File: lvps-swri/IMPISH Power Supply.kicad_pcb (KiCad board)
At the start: 4 copper layers, 90 x 90 mm, 68 parts, among them J1 Battery +, J2 Battery +, J3 Battery -, J4 Battery -, J5 BCS-117-L-D-TE, U1 PXG-M15-24WS05, U2 CCG30-24-12S, U3 PXC-M03-24WD15-A, U4 PXC-M03-24WS05-A, U5 PXG-M15-24WD05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

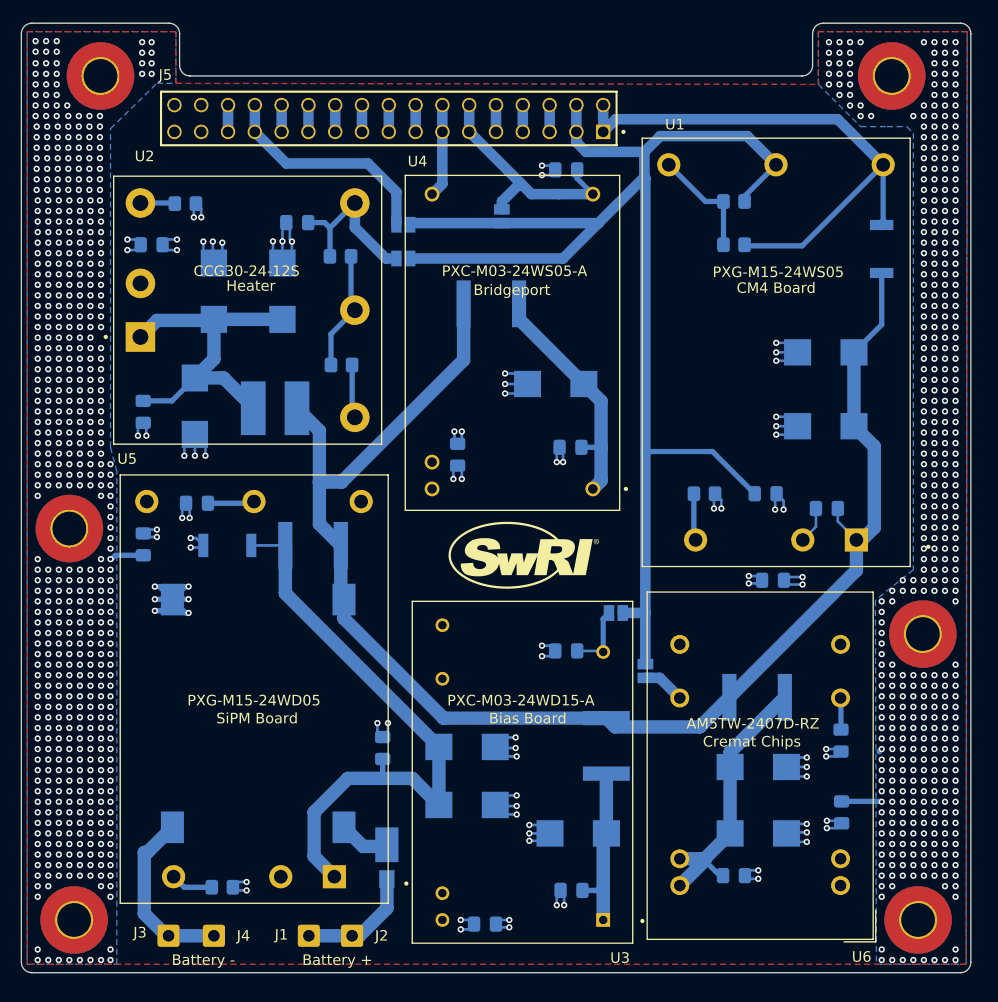
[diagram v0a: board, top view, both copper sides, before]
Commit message: swri lvps main: two layer board
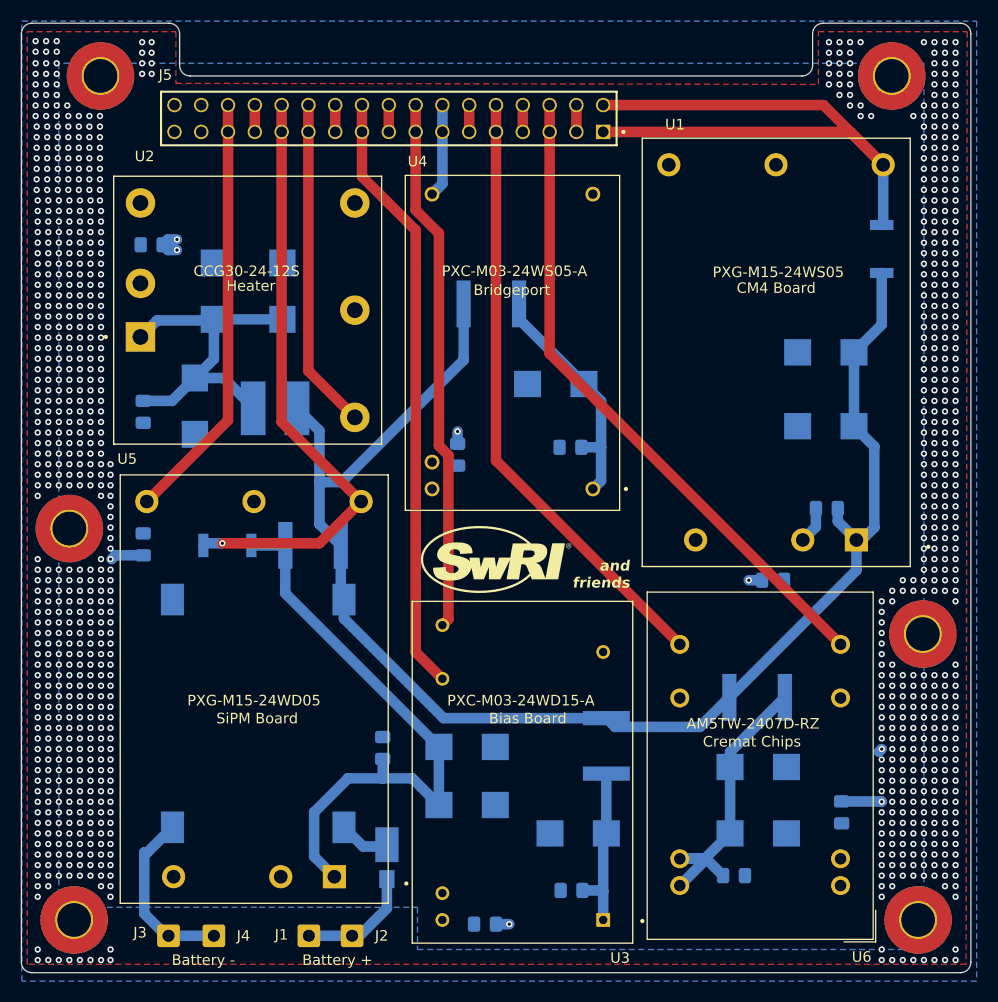
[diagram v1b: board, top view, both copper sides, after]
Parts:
- removed C12, C16, C20, C26, C31, C6: .01uF, Capacitor_SMD:C_0805_2012Metric_Pad1.18x1.45mm_HandSolder
- removed JP1, JP2, JP3, JP4, JP5: ~, Jumper:SolderJumper-2_P1.3mm_Open_Pad1.0x1.5mm
- removed R1, R2, R3: 0, Resistor_SMD:R_0805_2012Metric_Pad1.20x1.40mm_HandSolder
- removed R4, R5, R6, R7: DNI, Resistor_SMD:R_0805_2012Metric_Pad1.20x1.40mm_HandSolder
- moved G*** 2.65 mm to (205.4, 143.0)
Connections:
- J5 pad 03: GND1 -> GND
- J5 pad 04: GND1 -> GND
- J5 pad 07: Cremat GND -> GND
- J5 pad 08: Cremat GND -> GND
- J5 pad 11: Bridgeport GND -> GND
- J5 pad 12: Bridgeport GND -> GND
- J5 pad 17: Bias GND -> GND
- J5 pad 18: Bias GND -> GND
- J5 pad 21: Heater GND -> GND
- J5 pad 22: Heater GND -> GND
- J5 pad 27: SiPM GND -> GND
- J5 pad 28: SiPM GND -> GND
- U1 pad 3: Net-(U1-REMOTE_ON/OFF) -> GND
- U1 pad 5: GND1 -> GND
- U1 pad 6: Net-(U1-TRIM) -> unconnected-(U1-TRIM-Pad6)
- U2 pad 3: Net-(U2-RC) -> GND
- U2 pad 5: Net-(U2-TRM) -> unconnected-(U2-TRM-Pad5)
- U2 pad 6: Heater GND -> GND
- U3 pad 11: Bias GND -> GND
- U4 pad 12: Bridgeport GND -> GND
- U5 pad 3: Net-(U5-REMOTE_ON/OFF) -> GND
- U5 pad 5: SiPM GND -> GND
- U6 pad 16: Cremat GND -> GND
- U6 pad 9: Cremat GND -> GND
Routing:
- net GND1: track 135.3 -> 0.00 mm
- net Cremat GND: track 92.3 -> 0.00 mm
- net GND: track 110.7 -> 18.7 mm, vias 77 -> 0
- net Bias GND: track 76.5 -> 0.00 mm
- net SiPM GND: track 61.9 -> 0.00 mm
- net Heater GND: track 25.8 -> 0.00 mm
- net Bridgeport GND: track 22.8 -> 0.00 mm
- net Net-(U2-TRM): track 10.9 -> 0.00 mm
- net Net-(U1-TRIM): track 10.7 -> 0.00 mm
- net CM4 +5V: track 53.4 -> 62.5 mm
- net Heater 12V: track 36.1 -> 31.4 mm
- net Net-(U1-REMOTE_ON/OFF): track 4.22 -> 0.00 mm
- net Net-(U5-REMOTE_ON/OFF): track 4.03 -> 0.00 mm
- net SiPM +5V: track 60.8 -> 57.4 mm, vias 2 -> 1
- net Net-(U2-RC): track 3.20 -> 0.00 mm
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- added copper zone on B.Cu, net GND
- removed copper zone on In1.Cu, net GND
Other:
- copper layers 4 -> 2
- board text added: "and friends"

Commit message: swri lvps main: fix cap models
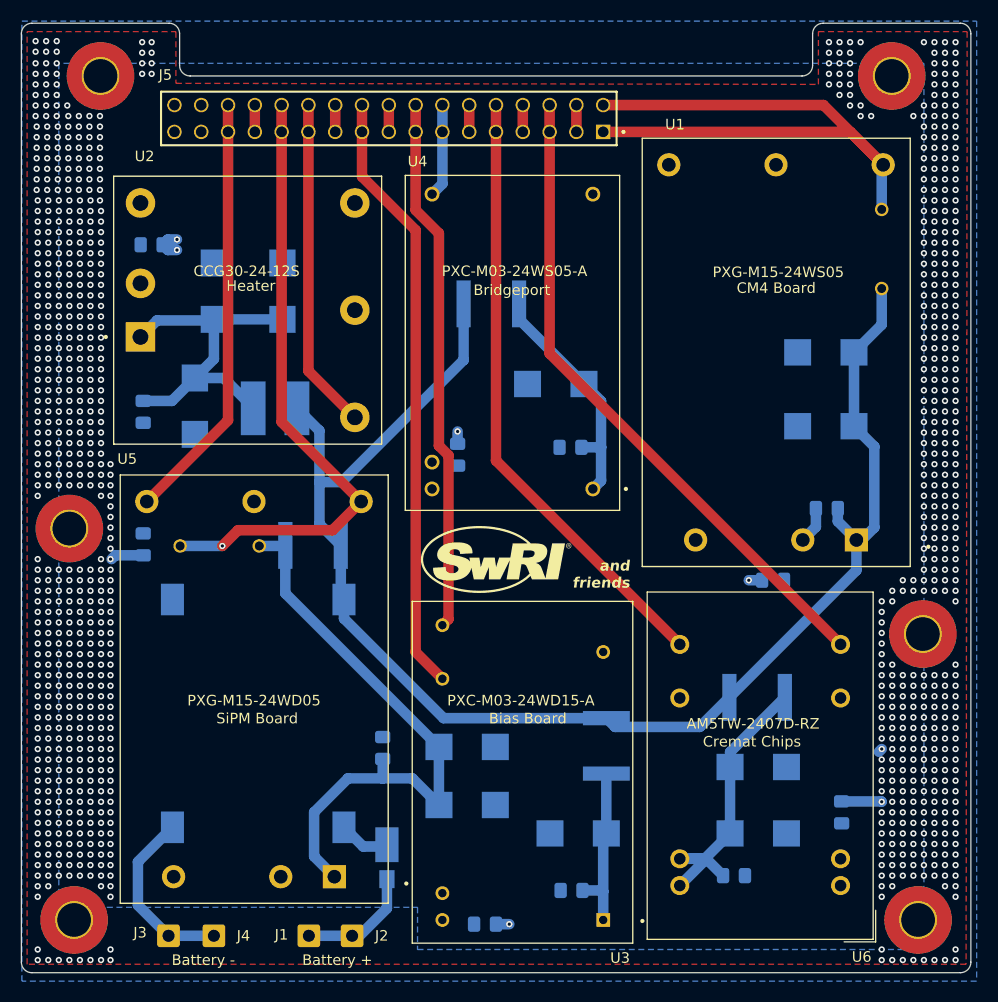
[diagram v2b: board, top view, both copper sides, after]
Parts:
- C1, C21: footprint IMPISH Library:CAPC4520X150N -> IMPISH Library:CAP_DE2B3SA101KN3AY02F
- moved C21 0.73 mm to (179.2, 141.8)
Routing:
- net SiPM +5V: track 57.4 -> 59.6 mm
- net CM4 +5V: track 62.5 -> 60.8 mm
- net Net-(U1-+VIN): track 138.4 -> 136.9 mm
- net Net-(U5-+VIN): track 56.8 -> 56.0 mm
